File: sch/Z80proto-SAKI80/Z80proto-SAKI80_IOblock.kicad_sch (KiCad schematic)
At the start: 37 parts, among them SW101 RESET, U101 LMC555, U14 AC541, U15 HC139, U17 TD62783, U18 TD62083, U21 23LC512, U4 HC138

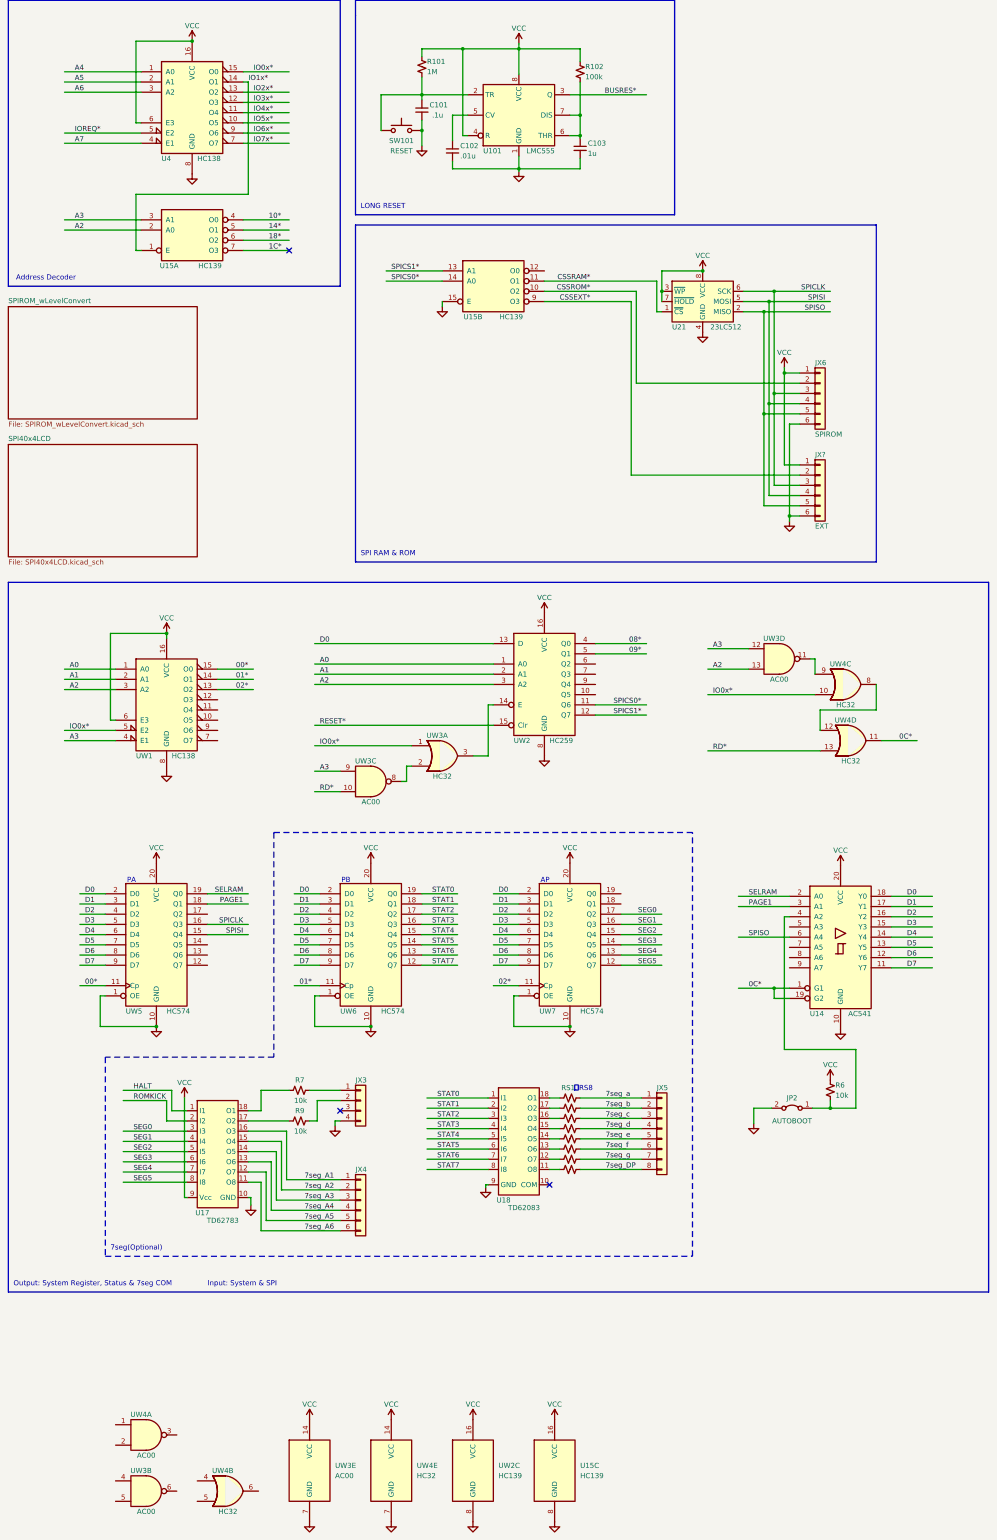
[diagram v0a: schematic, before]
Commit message: add SAKI80 support
add SAKI80(AKA Super AKI-80) support,
Modify Comand & intel HEX upload command to MiniLoader.
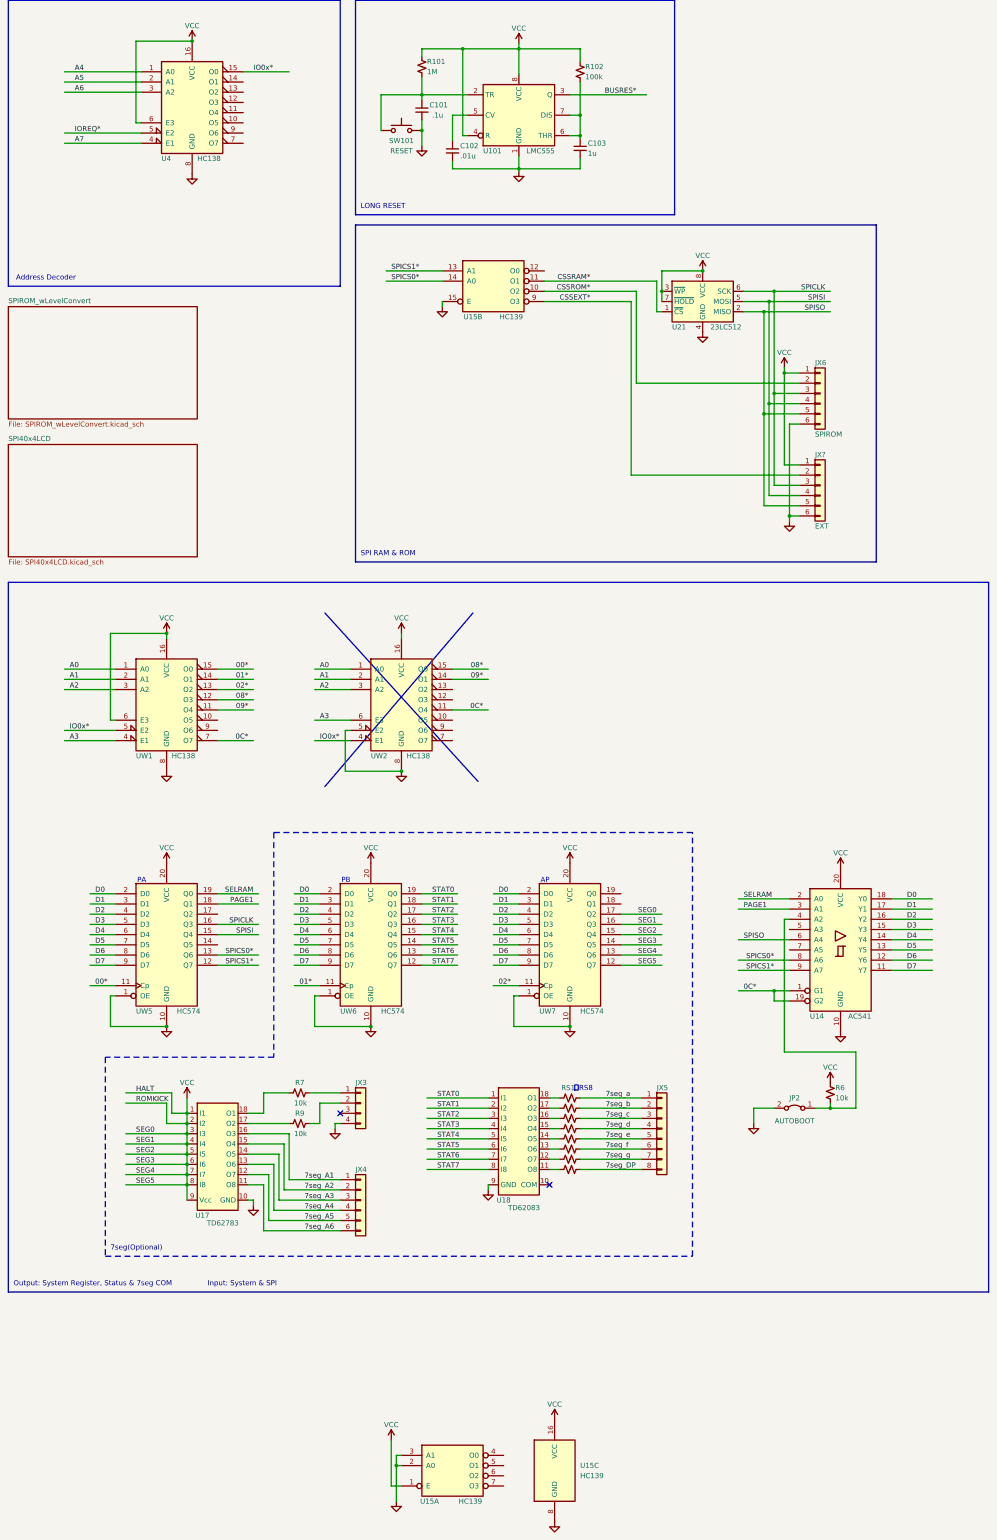
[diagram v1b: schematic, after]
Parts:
- removed UW2: HC139, symbol 74xx:74LS139
- removed UW3: AC00, symbol 74xx:74LS00
- removed UW4: HC32, symbol 74xx:74LS32
- added UW2: HC138, symbol 74xx:74LS138
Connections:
- net HALT is gone; now on net VCC: U17.1 (I1)
- net ROMKICK is gone; now on net VCC: U17.2 (I2)
- net SEG0 is gone; now on net VCC: U17.3 (I3), UW7.17 (Q2)
- net SEG1 is gone; now on net VCC: U17.4 (I4), UW7.16 (Q3)
- net SEG2 is gone; now on net VCC: U17.5 (I5), UW7.15 (Q4)
- net SEG3 is gone; now on net VCC: U17.6 (I6), UW7.14 (Q5)
- net SEG4 is gone; now on net VCC: U17.7 (I7), UW7.13 (Q6)
- net SEG5 is gone; now on net VCC: U17.8 (I8), UW7.12 (Q7)
- net 08*: now also UW1.12 (O3), UW2.15 (O0)
- net 09*: now also UW1.11 (O4), UW2.14 (O1)
- net 0C*: now also UW1.7 (O7), UW2.11 (O4)
- net A0: now also UW2.1 (A0)
- net A1: now also UW2.2 (A1)
- net A2: now also UW2.3 (A2); no longer U15.2 (A0)
- net A3: now also UW2.6 (E3); no longer U15.3 (A1)
- net GND: now also U15.2 (A0), U15.3 (A1), UW2.5 (E2), UW2.8 (GND)
- net IO0x*: now also UW2.4 (E1)
- net SPICS0*: now also U14.8 (A6), UW5.13 (Q6)
- net SPICS1*: now also U14.9 (A7), UW5.12 (Q7)
- net VCC: now also U15.1 (E), UW2.16 (VCC)
- net 10*: no longer names the net of U15.4 (O0)
- net 14*: no longer names the net of U15.5 (O1)
- net 18*: no longer names the net of U15.6 (O2)
- net 1C*: no longer names the net of U15.7 (O3)
- net IO1x*: no longer names the net of U4.14 (O1)
- net IO1x*: no longer U15.1 (E)
- net IO2x*: no longer names the net of U4.13 (O2)
- net IO3x*: no longer names the net of U4.12 (O3)
- net IO4x*: no longer names the net of U4.11 (O4)
- net IO5x*: no longer names the net of U4.10 (O5)
- net IO6x*: no longer names the net of U4.9 (O6)
- net IO7x*: no longer names the net of U4.7 (O7)
- no-connect marks 3 -> 2
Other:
- moved on the sheet: JP2, JX3, R6, R7, R9, U14, U15A, U17

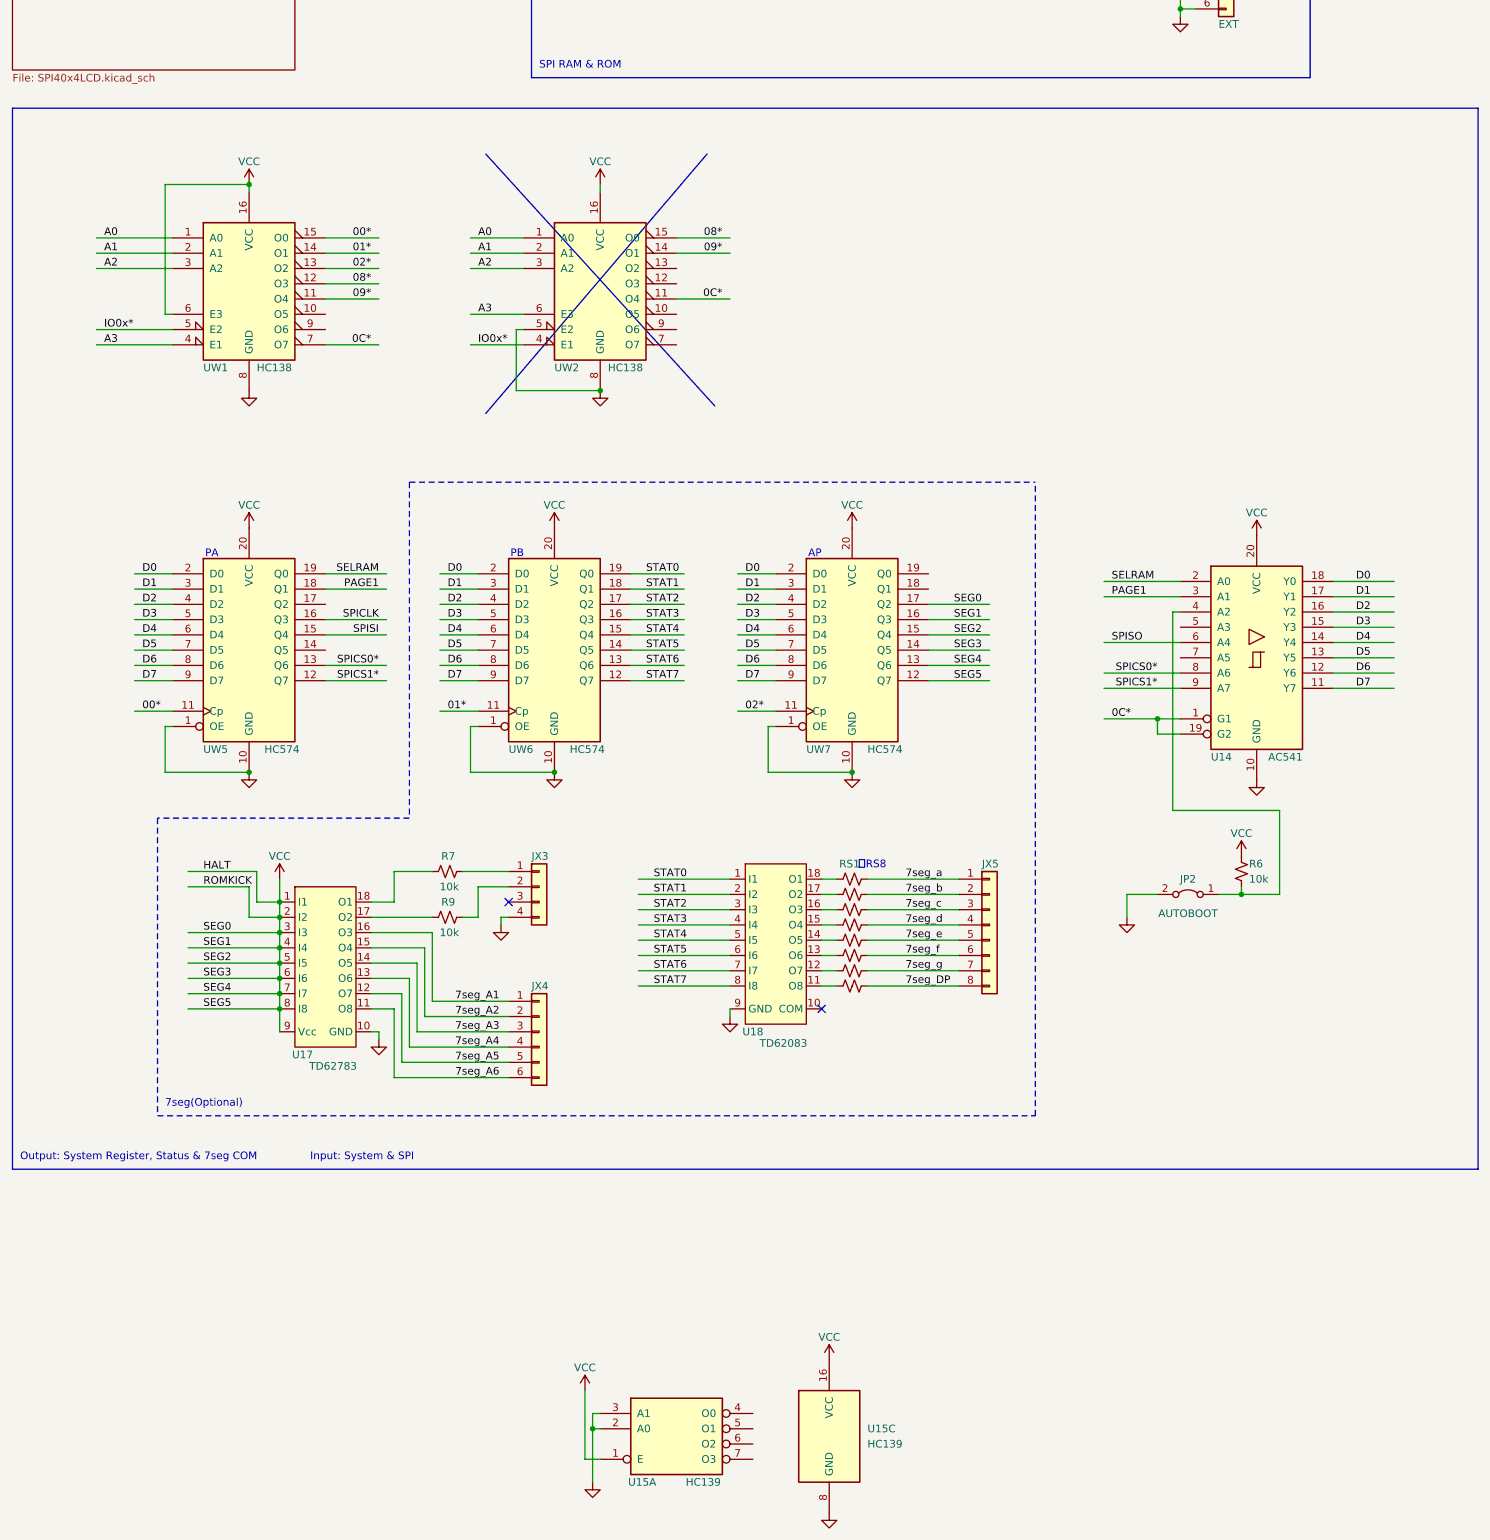
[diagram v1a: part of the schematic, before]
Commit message: add misc.
add SIO Hard flow control(but not work ...),
add WAIT implement,
add kermit implement(test).
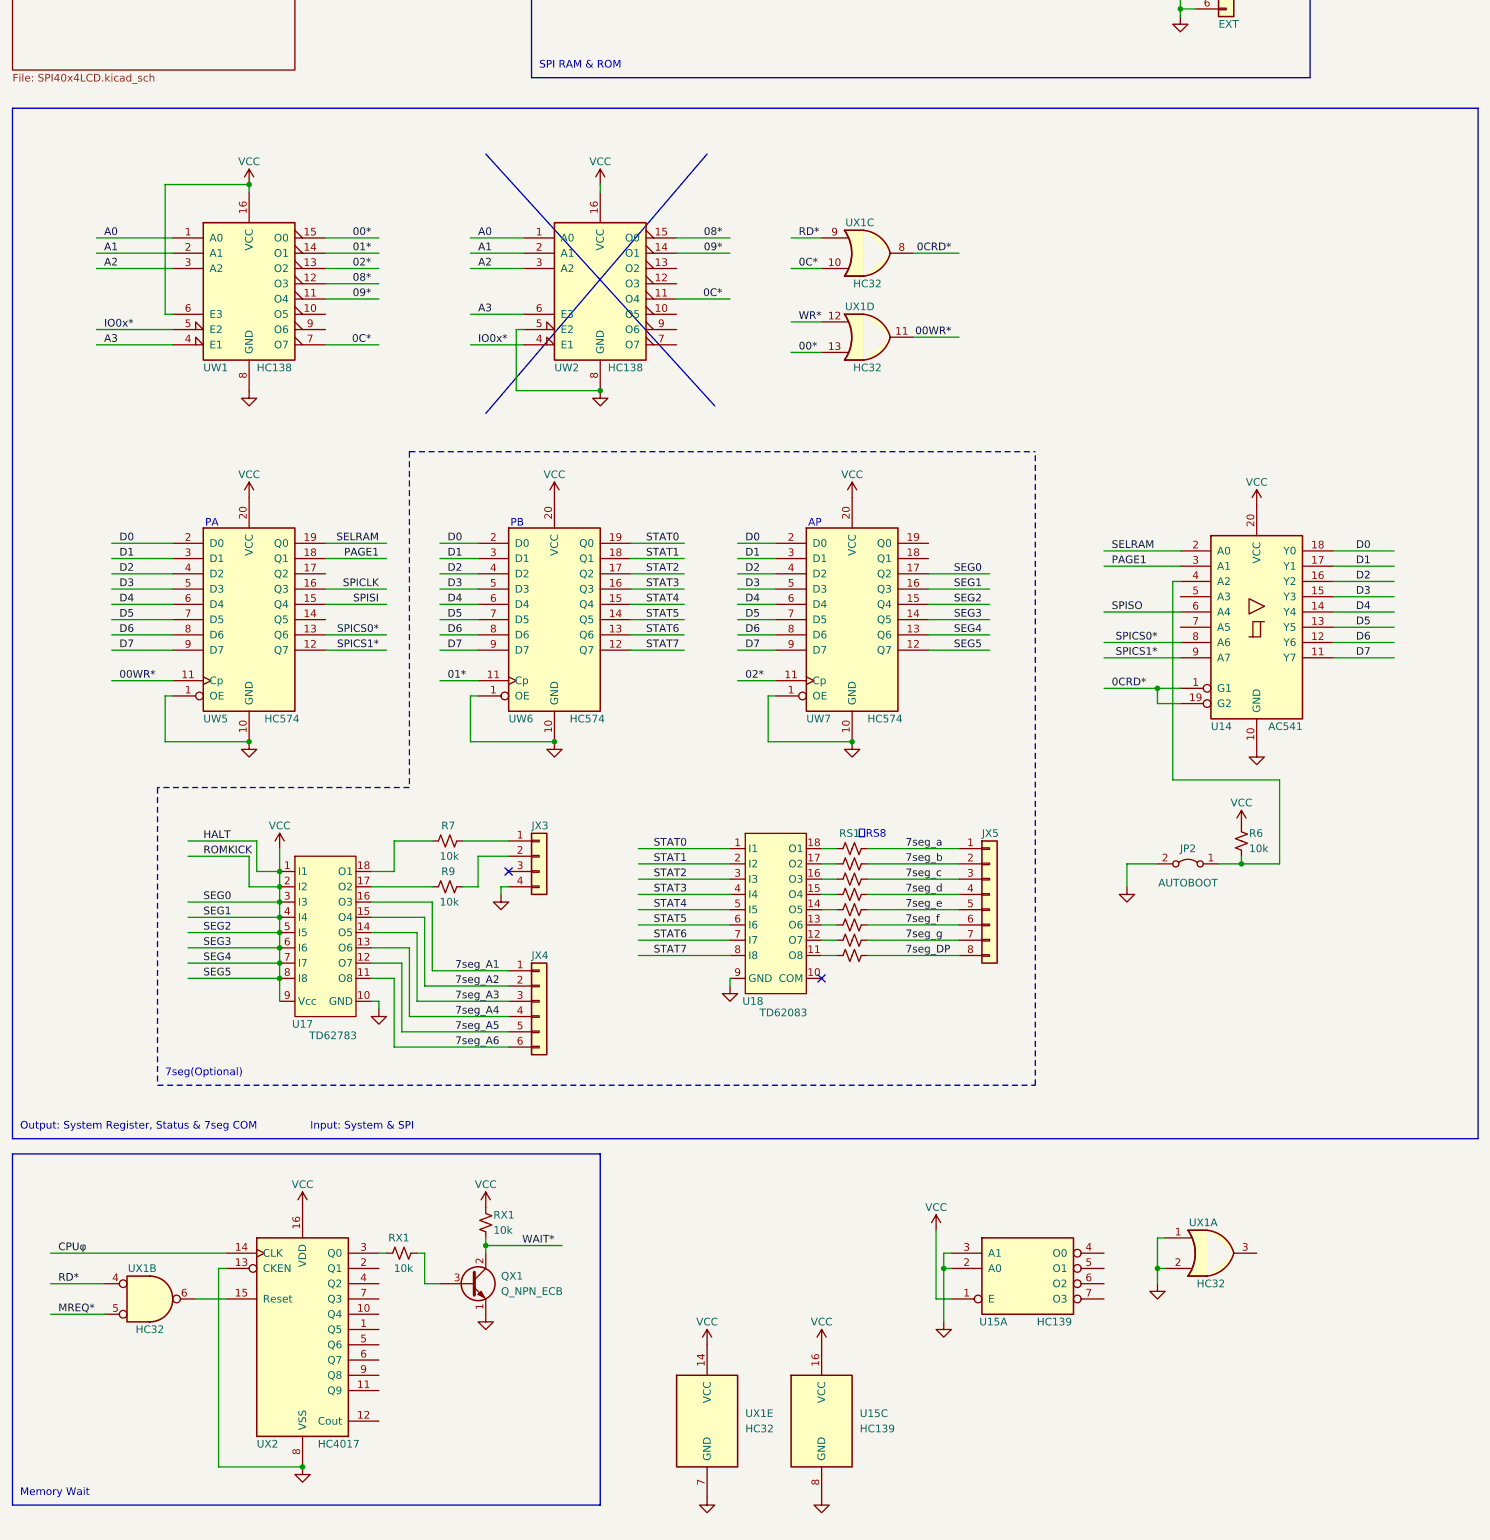
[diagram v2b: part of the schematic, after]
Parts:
- added QX1: Q_NPN_ECB, symbol Device:Q_NPN_ECB
- added RX1 (x2): 10k, symbol Device:R_Small_US
- added UX1: HC32, symbol 74xx:74LS32
- added UX2: HC4017, symbol 4xxx:4017
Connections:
- net 00*: now also UX1.13; no longer UW5.11 (Cp)
- net 0C*: now also UX1.10; no longer U14.1 (G1), U14.19 (G2)
- net GND: now also QX1.1 (E), UX1.1, UX1.2, UX1.7 (GND), UX2.13 (CKEN), UX2.8 (VSS)
- net VCC: now also RX1.1, UX1.14 (VCC), UX2.16 (VDD)
- new net: UX1.6, UX2.15 (Reset)
- new net: RX1.1, UX2.3 (Q0)
- new net: QX1.3 (B), RX1.2
- new net 00WR*: UW5.11 (Cp), UX1.11
- new net 0CRD*: U14.1 (G1), U14.19 (G2), UX1.8
- new net CPUφ: UX2.14 (CLK)
- new net MREQ*: UX1.5
- new net RD*: UX1.4, UX1.9
- new net WAIT*: QX1.2 (C), RX1.2
- new net WR*: UX1.12
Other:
- note added: "Memory Wait"
- moved on the sheet: JP2, JX3, JX4, JX5, R6, R7, R9, RS1, U14, U15A, U15C, U17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
